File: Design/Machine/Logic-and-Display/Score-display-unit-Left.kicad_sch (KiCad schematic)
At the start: 5 parts, among them M1 Red, M2 Red, M3 Red, M4 Red

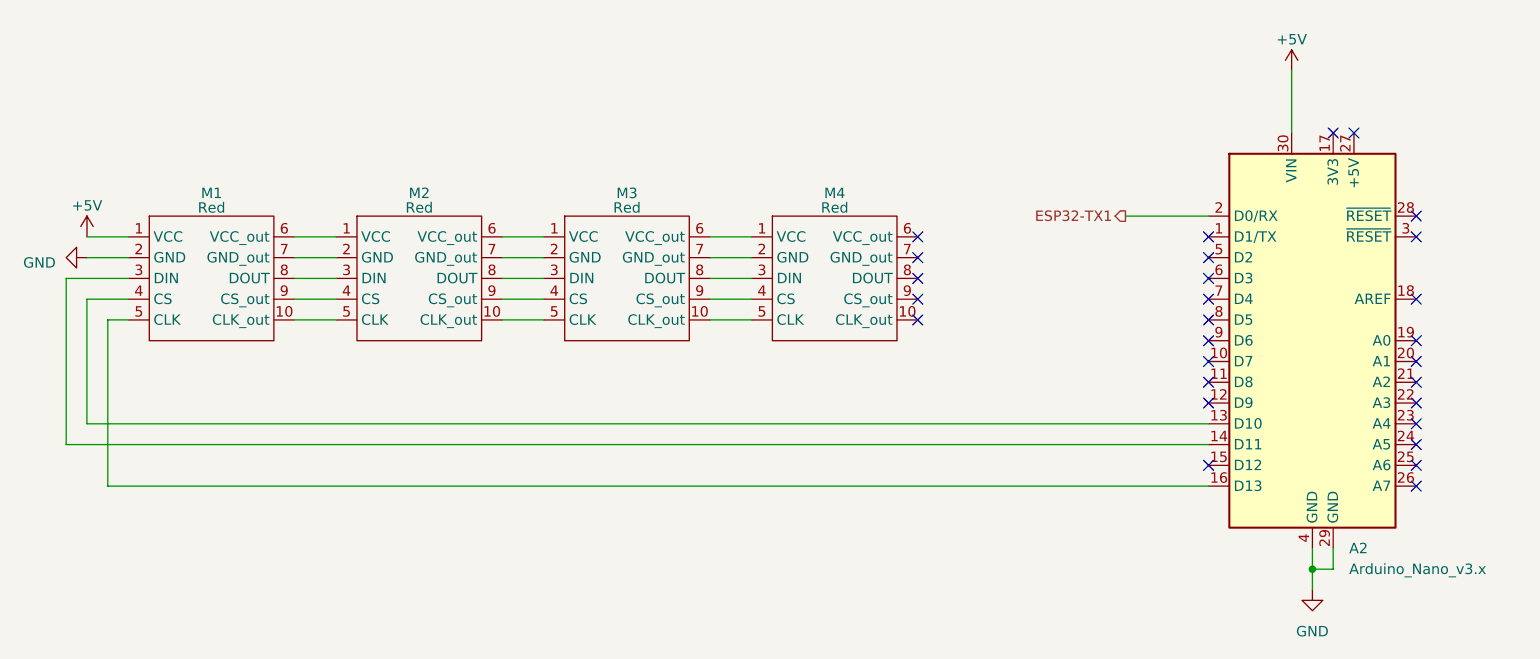
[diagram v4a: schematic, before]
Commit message: feat: logic and display units schecmatics
complete logic and display units schematics
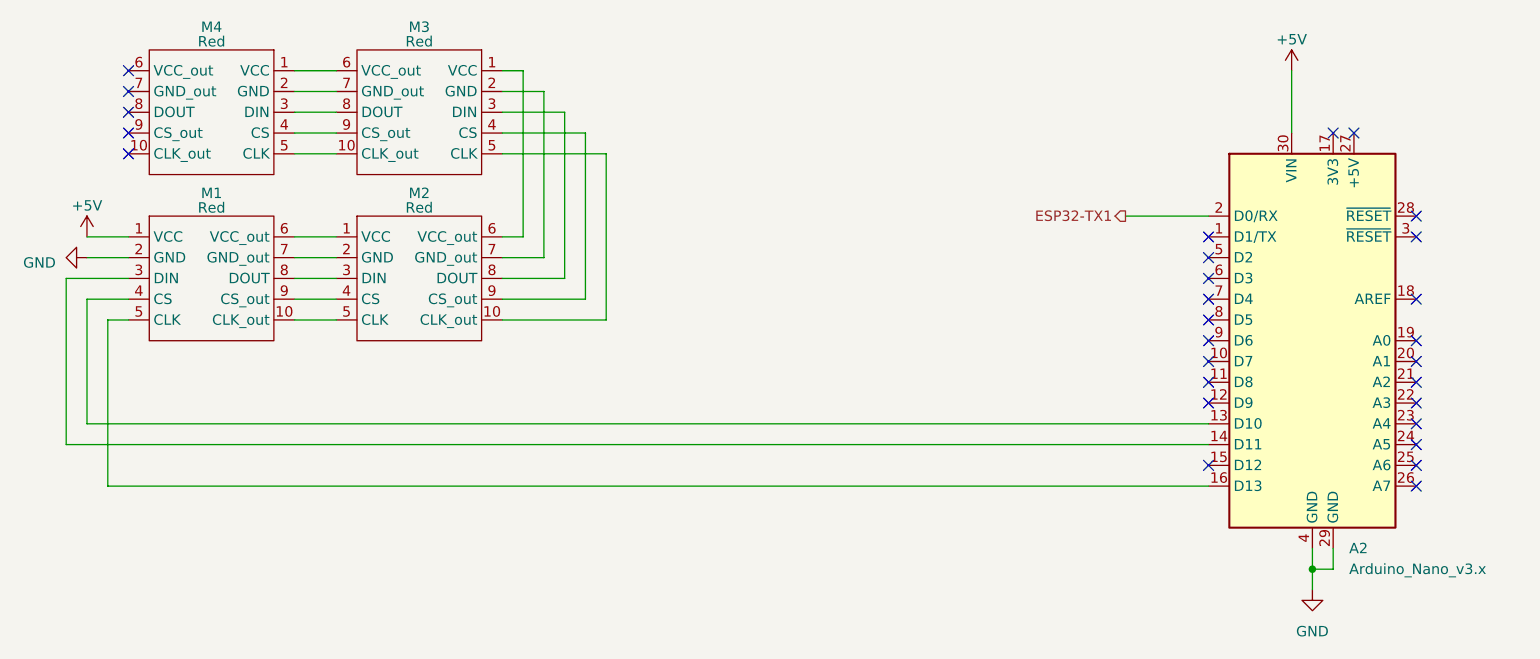
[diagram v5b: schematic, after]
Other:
- moved on the sheet: M3, M4
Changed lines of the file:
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@@
   (title_block
     (title "Left score display unit schematic")
-    (date "2023-05-19")
+    (date "2023-06-14")
     (rev "1.0.0")
     (comment 1 "Connection to logic unit pending")
@@
   )
   (no_connect (at 218.44 93.98))
-  (no_connect (at 157.48 86.36))
+  (no_connect (at 60.96 71.12))
   (no_connect (at 218.44 116.84))
+  (no_connect (at 60.96 68.58))
   (no_connect (at 193.04 88.9))
   (no_connect (at 193.04 91.44))
@@
   (no_connect (at 218.44 109.22))
   (no_connect (at 218.44 99.06))
-  (no_connect (at 157.48 93.98))
   (no_connect (at 218.44 83.82))
   (no_connect (at 218.44 104.14))
@@
   (no_connect (at 218.44 106.68))
   (no_connect (at 218.44 101.6))
-  (no_connect (at 157.48 88.9))
   (no_connect (at 193.04 86.36))
   (no_connect (at 218.44 111.76))
+  (no_connect (at 60.96 73.66))
+  (no_connect (at 60.96 66.04))
   (no_connect (at 218.44 114.3))
   (no_connect (at 193.04 93.98))
   (no_connect (at 210.82 73.66))
-  (no_connect (at 157.48 96.52))
+  (no_connect (at 60.96 76.2))
   (no_connect (at 218.44 86.36))
-  (no_connect (at 157.48 91.44))
   (no_connect (at 193.04 104.14))
   (no_connect (at 193.04 101.6))
@@
     (stroke (width 0) (type default))
   )
-  (wire (pts (xy 106.68 91.44) (xy 111.76 91.44))
+  (wire (pts (xy 116.84 93.98) (xy 116.84 73.66))
+    (stroke (width 0) (type default))
+  )
+  (wire (pts (xy 109.22 86.36) (xy 109.22 66.04))
+    (stroke (width 0) (type default))
+  )
+  (wire (pts (xy 106.68 96.52) (xy 119.38 96.52))
+    (stroke (width 0) (type default))
+  )
+  (wire (pts (xy 106.68 93.98) (xy 116.84 93.98))
+    (stroke (width 0) (type default))
+  )
+  (wire (pts (xy 111.76 88.9) (xy 111.76 68.58))
     (stroke (width 0) (type default))
   )
@@
     (stroke (width 0) (type default))
   )
+  (wire (pts (xy 111.76 68.58) (xy 106.68 68.58))
+    (stroke (width 0) (type default))
+  )
   (wire (pts (xy 208.28 127) (xy 205.74 127))
     (stroke (width 0) (type default))
@@
     (stroke (width 0) (type default))
   )
+  (wire (pts (xy 81.28 73.66) (xy 86.36 73.66))
+    (stroke (width 0) (type default))
+  )
   (wire (pts (xy 205.74 127) (xy 205.74 129.54))
     (stroke (width 0) (type default))
   )
+  (wire (pts (xy 81.28 71.12) (xy 86.36 71.12))
+    (stroke (width 0) (type default))
+  )
+  (wire (pts (xy 208.28 124.46) (xy 208.28 127))
+    (stroke (width 0) (type default))
+  )
+  (wire (pts (xy 81.28 76.2) (xy 86.36 76.2))
+    (stroke (width 0) (type default))
+  )
+  (wire (pts (xy 106.68 91.44) (xy 114.3 91.44))
+    (stroke (width 0) (type default))
+  )
+  (wire (pts (xy 182.88 83.82) (xy 193.04 83.82))
+    (stroke (width 0) (type default))
+  )
+  (wire (pts (xy 81.28 86.36) (xy 86.36 86.36))
+    (stroke (width 0) (type default))
+  )
+  (wire (pts (xy 193.04 109.22) (xy 55.88 109.22))
+    (stroke (width 0) (type default))
+  )
+  (wire (pts (xy 81.28 93.98) (xy 86.36 93.98))
+    (stroke (width 0) (type default))
+  )
+  (wire (pts (xy 81.28 68.58) (xy 86.36 68.58))
+    (stroke (width 0) (type default))
+  )
+  (wire (pts (xy 114.3 71.12) (xy 106.68 71.12))
+    (stroke (width 0) (type default))
+  )
+  (wire (pts (xy 55.88 109.22) (xy 55.88 93.98))
+    (stroke (width 0) (type default))
+  )
+  (wire (pts (xy 114.3 91.44) (xy 114.3 71.12))
+    (stroke (width 0) (type default))
+  )
+  (wire (pts (xy 116.84 73.66) (xy 106.68 73.66))
+    (stroke (width 0) (type default))
+  )
+  (wire (pts (xy 205.74 124.46) (xy 205.74 127))
+    (stroke (width 0) (type default))
+  )
+  (wire (pts (xy 119.38 96.52) (xy 119.38 76.2))
+    (stroke (width 0) (type default))
+  )
+  (wire (pts (xy 81.28 91.44) (xy 86.36 91.44))
+    (stroke (width 0) (type default))
+  )
+  (wire (pts (xy 58.42 96.52) (xy 60.96 96.52))
+    (stroke (width 0) (type default))
+  )
+  (wire (pts (xy 119.38 76.2) (xy 106.68 76.2))
+    (stroke (width 0) (type default))
+  )
+  (wire (pts (xy 109.22 66.04) (xy 106.68 66.04))
+    (stroke (width 0) (type default))
+  )
+  (wire (pts (xy 58.42 116.84) (xy 58.42 96.52))
+    (stroke (width 0) (type default))
+  )
+  (wire (pts (xy 55.88 93.98) (xy 60.96 93.98))
+    (stroke (width 0) (type default))
+  )
+  (wire (pts (xy 106.68 86.36) (xy 109.22 86.36))
+    (stroke (width 0) (type default))
+  )
+  (wire (pts (xy 53.34 91.44) (xy 60.96 91.44))
+    (stroke (width 0) (type default))
+  )
+  (wire (pts (xy 193.04 111.76) (xy 53.34 111.76))
+    (stroke (width 0) (type default))
+  )
   (wire (pts (xy 106.68 88.9) (xy 111.76 88.9))
     (stroke (width 0) (type default))
   )
-  (wire (pts (xy 208.28 124.46) (xy 208.28 127))
-    (stroke (width 0) (type default))
-  )
-  (wire (pts (xy 132.08 93.98) (xy 137.16 93.98))
-    (stroke (width 0) (type default))
-  )
-  (wire (pts (xy 132.08 88.9) (xy 137.16 88.9))
-    (stroke (width 0) (type default))
-  )
-  (wire (pts (xy 132.08 91.44) (xy 137.16 91.44))
-    (stroke (width 0) (type default))
-  )
-  (wire (pts (xy 182.88 83.82) (xy 193.04 83.82))
-    (stroke (width 0) (type default))
-  )
-  (wire (pts (xy 81.28 86.36) (xy 86.36 86.36))
-    (stroke (width 0) (type default))
-  )
-  (wire (pts (xy 193.04 109.22) (xy 55.88 109.22))
-    (stroke (width 0) (type default))
-  )
-  (wire (pts (xy 81.28 93.98) (xy 86.36 93.98))
-    (stroke (width 0) (type default))
-  )
-  (wire (pts (xy 55.88 109.22) (xy 55.88 93.98))
-    (stroke (width 0) (type default))
-  )
-  (wire (pts (xy 106.68 93.98) (xy 111.76 93.98))
-    (stroke (width 0) (type default))
-  )
-  (wire (pts (xy 205.74 124.46) (xy 205.74 127))
-    (stroke (width 0) (type default))
-  )
-  (wire (pts (xy 106.68 96.52) (xy 111.76 96.52))
-    (stroke (width 0) (type default))
-  )
-  (wire (pts (xy 81.28 91.44) (xy 86.36 91.44))
-    (stroke (width 0) (type default))
-  )
-  (wire (pts (xy 58.42 96.52) (xy 60.96 96.52))
-    (stroke (width 0) (type default))
-  )
-  (wire (pts (xy 132.08 86.36) (xy 137.16 86.36))
-    (stroke (width 0) (type default))
-  )
-  (wire (pts (xy 132.08 96.52) (xy 137.16 96.52))
-    (stroke (width 0) (type default))
-  )
-  (wire (pts (xy 58.42 116.84) (xy 58.42 96.52))
-    (stroke (width 0) (type default))
-  )
-  (wire (pts (xy 55.88 93.98) (xy 60.96 93.98))
-    (stroke (width 0) (type default))
-  )
-  (wire (pts (xy 53.34 91.44) (xy 60.96 91.44))
-    (stroke (width 0) (type default))
-  )
-  (wire (pts (xy 193.04 111.76) (xy 53.34 111.76))
-    (stroke (width 0) (type default))
-  )
-  (wire (pts (xy 106.68 86.36) (xy 111.76 86.36))
-    (stroke (width 0) (type default))
-  )
   (wire (pts (xy 81.28 96.52) (xy 86.36 96.52))
+    (stroke (width 0) (type default))
+  )
+  (wire (pts (xy 81.28 66.04) (xy 86.36 66.04))
     (stroke (width 0) (type default))
   )
@@
     )
   )
-  (symbol (lib_id "Arduino modules:8x8_LED_Matrix_MAX7219") (at 121.92 81.28 0) (unit 1)
+  (symbol (lib_id "Arduino modules:8x8_LED_Matrix_MAX7219") (at 96.52 60.96 0) (mirror y) (unit 1)
     (in_bom yes) (on_board yes) (dnp no)
-    (property "Reference" "M3" (at 121.92 81.026 0)
-      (effects (font (size 1.27 1.27)))
-    )
-    (property "Value" "Red" (at 121.92 82.804 0)
-      (effects (font (size 1.27 1.27)))
-    )
-    (property "Footprint" "" (at 121.92 81.28 0)
-      (effects (font (size 1.27 1.27)) hide)
-    )
-    (property "Datasheet" "" (at 121.92 81.28 0)
+    (property "Reference" "M3" (at 96.52 60.706 0)
+      (effects (font (size 1.27 1.27)))
+    )
+    (property "Value" "Red" (at 96.52 62.484 0)
+      (effects (font (size 1.27 1.27)))
+    )
+    (property "Footprint" "" (at 96.52 60.96 0)
+      (effects (font (size 1.27 1.27)) hide)
+    )
+    (property "Datasheet" "" (at 96.52 60.96 0)
       (effects (font (size 1.27 1.27)) hide)
     )
@@
     )
   )
-  (symbol (lib_id "Arduino modules:8x8_LED_Matrix_MAX7219") (at 147.32 81.28 0) (unit 1)
+  (symbol (lib_id "Arduino modules:8x8_LED_Matrix_MAX7219") (at 71.12 60.96 0) (mirror y) (unit 1)
     (in_bom yes) (on_board yes) (dnp no)
-    (property "Reference" "M4" (at 147.32 81.026 0)
-      (effects (font (size 1.27 1.27)))
-    )
-    (property "Value" "Red" (at 147.32 82.804 0)
-      (effects (font (size 1.27 1.27)))
-    )
-    (property "Footprint" "" (at 147.32 81.28 0)
-      (effects (font (size 1.27 1.27)) hide)
-    )
-    (property "Datasheet" "" (at 147.32 81.28 0)
-      (effects (font (size 1.27 1.27)) hide)
-    )
+    (property "Reference" "M4" (at 71.12 60.706 0)
+      (effects (font (size 1.27 1.27)))
+    )
+    (property "Value" "Red" (at 71.12 62.484 0)
+      (effects (font (size 1.27 1.27)))
+    )
+    (property "Footprint" "" (at 71.12 60.96 0)
+      (effects (font (size 1.27 1.27)) hide)
+    )
+    (property "Datasheet" "" (at 71.12 60.96 0)
+      (effects (font (size 1.27 1.27)) hide)
+    )

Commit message: fix: set FC-16 hardware module variable
set hardware variable as FC-16, this stops flipping of the lower zone, fix wiring diagram to represent this
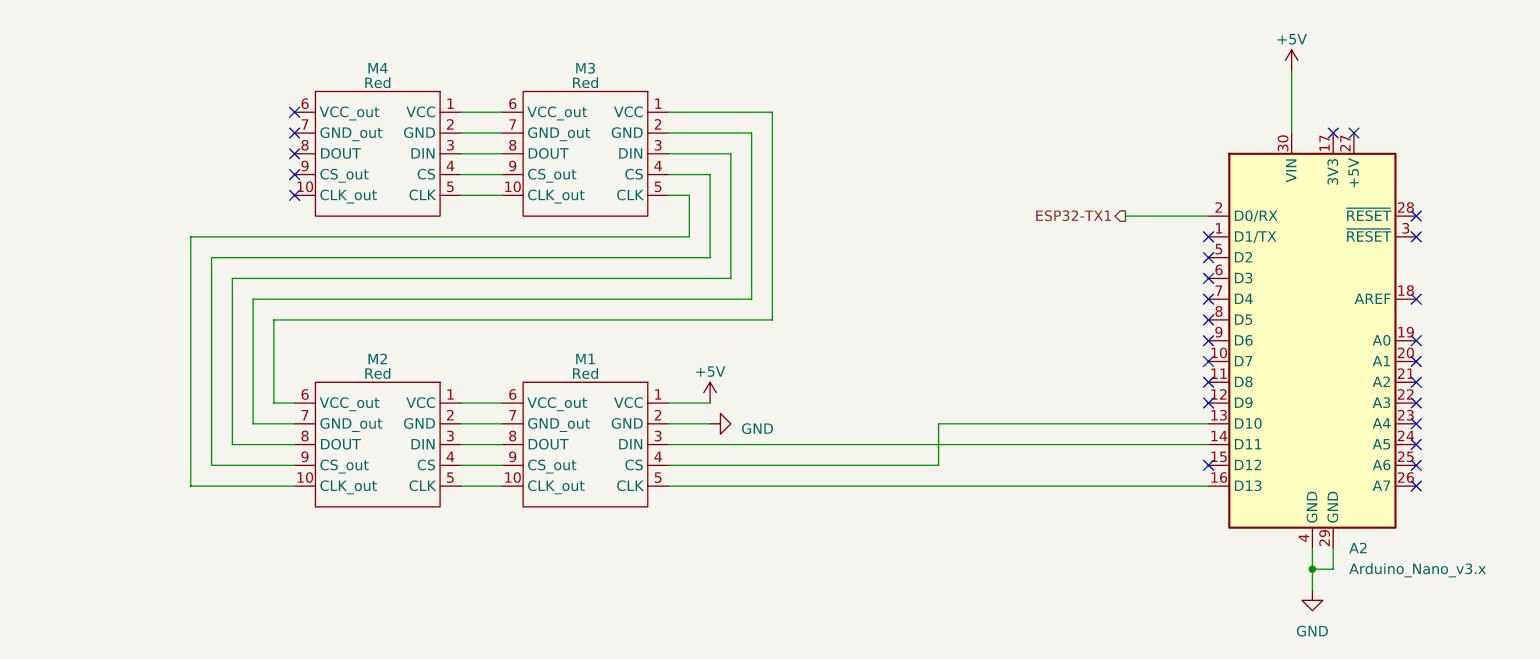
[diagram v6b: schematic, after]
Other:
- moved on the sheet: M1, M2, M3, M4
